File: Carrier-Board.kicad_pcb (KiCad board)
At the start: 4 copper layers, 92 x 96 mm, 59 parts, among them J1 CONN_3-6318491-6, J10 Conn_02x03_Odd_Even, J2 Conn_01x0, J4 SI-51009-F, J6 Conn_01x03_Male, J7 Conn_01x03_Male, J8 Conn_01x06_Male, J9 Conn_02x04_Odd_Even, SW1 SW_Push, SW2 SW_Push, SW3 SW_Push, U1 MPM3620, U2 MPM3620, m1 MountingHole_2.7mm_M2.5_Pad, m2 MountingHole_2.7mm_M2.5_Pad

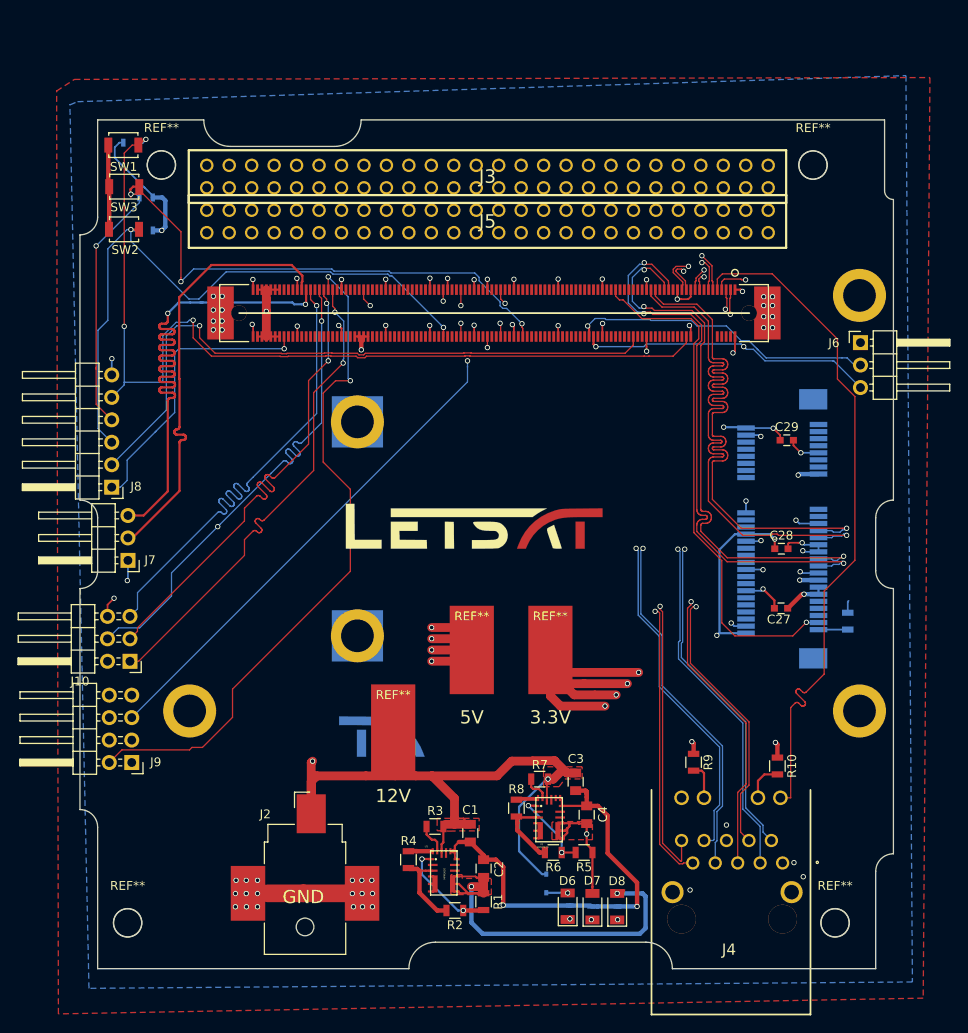
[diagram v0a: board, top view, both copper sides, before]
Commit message: Finished USB>rs232
Verify needed
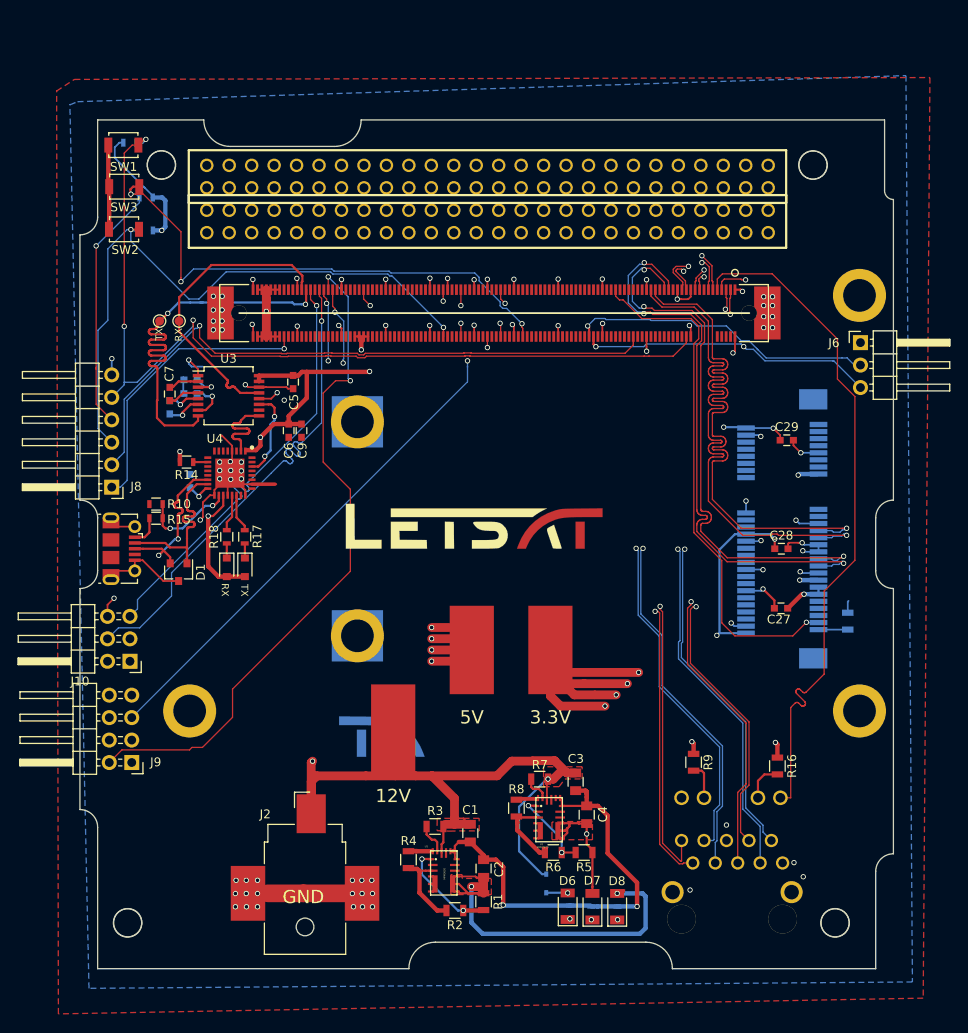
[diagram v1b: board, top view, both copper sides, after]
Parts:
- removed J7: Conn_01x03_Male, Pin_Headers:Pin_Header_Angled_1x03_Pitch2.54mm
- added C10: .1uF, Capacitors_SMD:C_0603, B.Cu at (94.4, 64.8)
- added C11: .33uF, Capacitors_SMD:C_0603, B.Cu at (94.4, 53.4)
- added C12: .33uF, Capacitors_SMD:C_0603, B.Cu at (94.4, 55.0)
- added C5: .1uF, Capacitors_SMD:C_0603, F.Cu at (106.0, 53.6)
- added C6: .1uF, Capacitors_SMD:C_0603, F.Cu at (105.5, 59.1)
- added C7: 47nF, Capacitors_SMD:C_0603, F.Cu at (92.1, 55.0)
- added C8: .33uF, Capacitors_SMD:C_0603, B.Cu at (92.1, 56.5)
- added C9: 4.7uF, Capacitors_SMD:C_0603, F.Cu at (107.0, 59.1)
- added D1: PESD12VL2BT,215, Diodes_SMD:D_SOT-23_NKA, F.Cu at (93.1, 75.2)
- added D2: LED, Diodes_SMD:D_0805, F.Cu at (100.6, 74.6)
- added D3: LED, Diodes_SMD:D_0805, F.Cu at (98.5, 74.6)
- added J11: USB_B_Micro, Connectors_USB:USB_Micro-B_Molex-105017-0001, F.Cu at (85.8, 72.5)
- added R10: 10K, Resistors_SMD:R_0603, F.Cu at (90.5, 67.5)
- added R14: 10K, Resistors_SMD:R_0603, F.Cu at (94.0, 62.7)
- added R15: 4.7K, Resistors_SMD:R_0603, F.Cu at (90.5, 69.0)
- added R17: 200, Resistors_SMD:R_0603, F.Cu at (100.6, 71.2)
- added R18: 200, Resistors_SMD:R_0603, F.Cu at (98.5, 71.2)
- added REF**: TestPoint_Pad_D1.0mm, TestPoint:TestPoint_Pad_D1.0mm, F.Cu at (93.1, 46.8)
- added REF**: TestPoint_Pad_D1.0mm, TestPoint:TestPoint_Pad_D1.0mm, F.Cu at (90.9, 46.8)
- added U3: MAX3221, Housings_SSOP:SSOP-16_5.3x6.2mm_Pitch0.65mm, F.Cu at (98.7, 55.2)
- added U4: FT232RQ, FT232RQ:QFN50P500X500X100-33N, F.Cu at (98.9, 64.0)
- J3, J5: value (none) -> Conn_02x26_Odd_Even
- U9: value (none) -> MSATA-Socket
- renumbered R10 to R16
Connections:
- C27 pad 1: +3.3V -> Net-(C27-Pad1)
- C28 pad 1: +3.3V -> Net-(C28-Pad1)
- C29 pad 1: +3.3V -> Net-(C29-Pad1)
- J1 pad 223: GBE0_CTREF(GND) -> (no net)
- J1 pad 224: GBE0_CTREF(GND) -> (no net)
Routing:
- net mCOM_5V_SBY: track 182.1 -> 245.1 mm, vias 8 -> 12
- net GBE0_CTREF(GND): track 191.3 -> 234.0 mm, vias 84 -> 81
- net Net-(D1-Pad1): track 0.00 -> 22.0 mm
- net Net-(D1-Pad2): track 0.00 -> 19.2 mm, vias 0 -> 2
- net mCOM_TX: track 64.6 -> 47.7 mm
- net mCOM_RX: track 48.9 -> 34.0 mm
- net Reset#: track 0.00 -> 10.7 mm, vias 0 -> 2
- net RXD: track 0.00 -> 10.4 mm
- net TXD: track 0.00 -> 10.0 mm, vias 0 -> 2
- net (no net): track 0.00 -> 6.57 mm, vias 0 -> 16
- net SPI_CS#: track 55.2 -> 49.1 mm
- net Net-(C12-Pad1): track 0.00 -> 4.56 mm, vias 0 -> 1
- net Net-(R17-Pad2): track 0.00 -> 4.34 mm
- net Net-(R18-Pad2): track 0.00 -> 4.20 mm
- net Net-(C8-Pad2): track 0.00 -> 3.96 mm, vias 0 -> 1
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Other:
- board text added: "RX"
- board text added: "TX"

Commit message: changed serial number
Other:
- board text added: "S/N: 0C137_v2"
- board text removed: "S/N: 0C137"

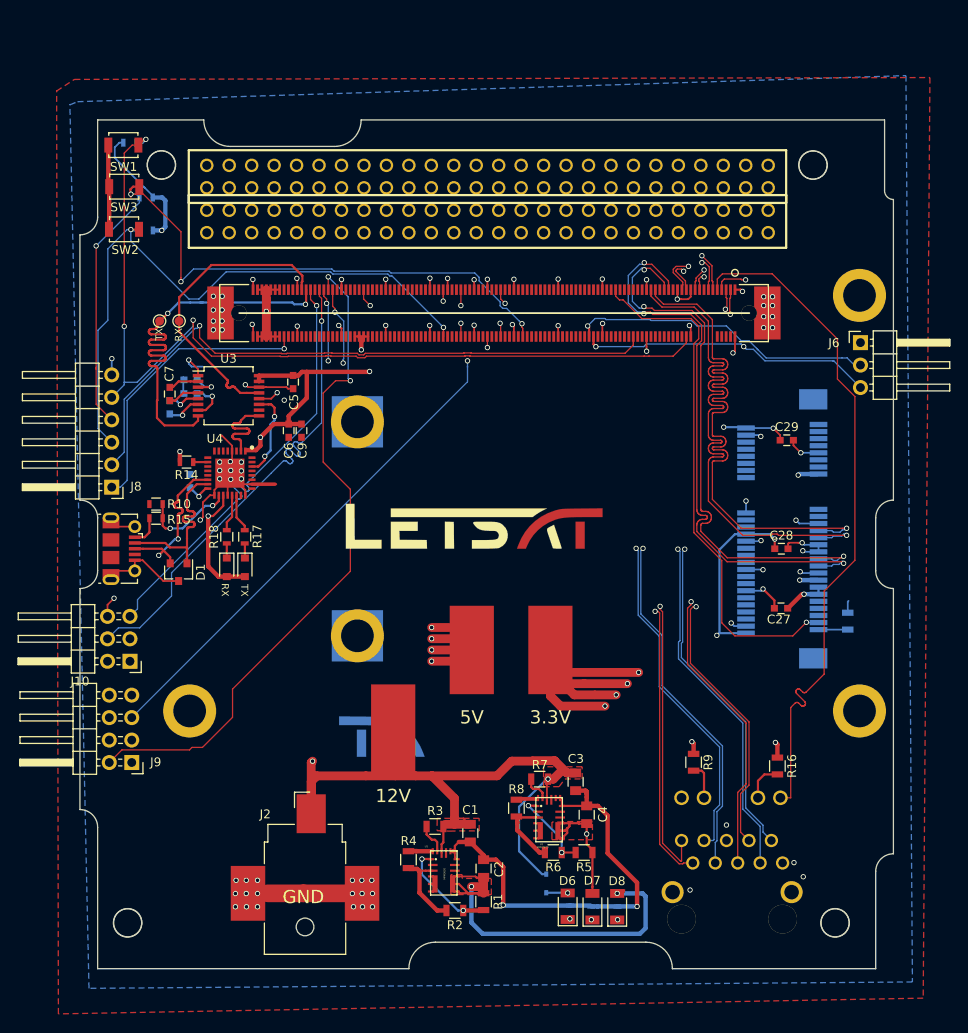
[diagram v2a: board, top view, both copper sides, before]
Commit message: Change footprint sizes
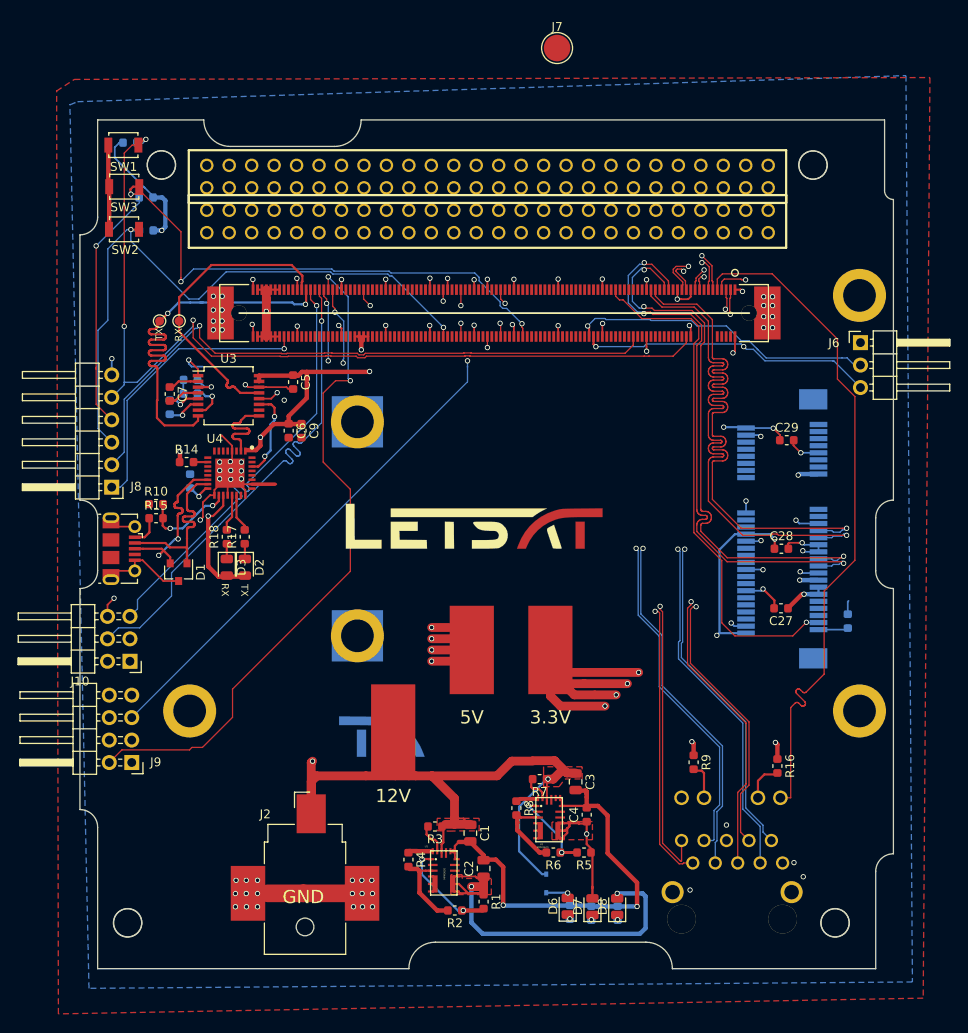
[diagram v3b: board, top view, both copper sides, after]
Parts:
- added J7: Conn_01x03_Male, TestPoint:TestPoint_Pad_D3.0mm, F.Cu at (135.9, 15.9)
- C1, C2, C3: footprint Capacitors_SMD:C_0805 -> Capacitor_SMD:C_0805_2012Metric
- C10, C11, C12, C27, C28, C29, C5, C6, C7, C8, C9: footprint Capacitors_SMD:C_0603 -> Capacitor_SMD:C_0603_1608Metric
- C4: footprint Capacitors_SMD:C_0805 -> Capacitor_SMD:C_0603_1608Metric
- D2, D3: footprint Diodes_SMD:D_0805 -> Diode_SMD:D_0805_2012Metric
- D6, D7, D8: footprint Diodes_SMD:D_1206 -> Diode_SMD:D_0805_2012Metric
- G1: footprint BusSimulator:LetSatLogo440 -> Carrier-Board:LetSat_Logo_440
- J1: footprint BusSimulator:ComExpressMini10 -> Carrier-Board:ComExpressMini10
- R1, R16, R2, R3, R32, R4, R5, R6, R7, R8, R9: footprint Resistors_SMD:R_0805 -> Resistor_SMD:R_0603_1608Metric
- R10, R11, R12, R13, R14, R15, R17, R18, R23, R24, R25: footprint Resistors_SMD:R_0603 -> Resistor_SMD:R_0603_1608Metric
- U1, U2: footprint BusSimulator:QFN-20 -> Carrier-Board:QFN-20
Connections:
- C27 pad 1: Net-(C27-Pad1) -> +3.3V
- C28 pad 1: Net-(C28-Pad1) -> +3.3V
- C29 pad 1: Net-(C29-Pad1) -> +3.3V
- J2 pad 3: GBE0_CTREF(GND) -> (no net)
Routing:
- net mCOM_12V: track 148.1 -> 155.2 mm
- net Net-(R5-Pad2): track 9.35 -> 11.3 mm
- net mCOM_5V_SBY: track 245.1 -> 243.8 mm
- net GNDA: track 19.7 -> 21.0 mm
- net +3.3V: track 245.6 -> 246.8 mm
- net Net-(R8-Pad1): track 5.00 -> 5.61 mm
- net Net-(D6-Pad1): track 0.00 -> 0.59 mm
- net Net-(D7-Pad1): track 0.00 -> 0.59 mm
- net Net-(D5-Pad2): track 2.44 -> 3.00 mm
- net Net-(D8-Pad1): track 0.00 -> 0.56 mm
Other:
- net class Default: clearance 0.2 -> 0.15
- net class Power: clearance 0.2 -> 0.15
- net class Signal: clearance 0.2 -> 0.15
- rule trace_clearance: 0.2 -> 0.15

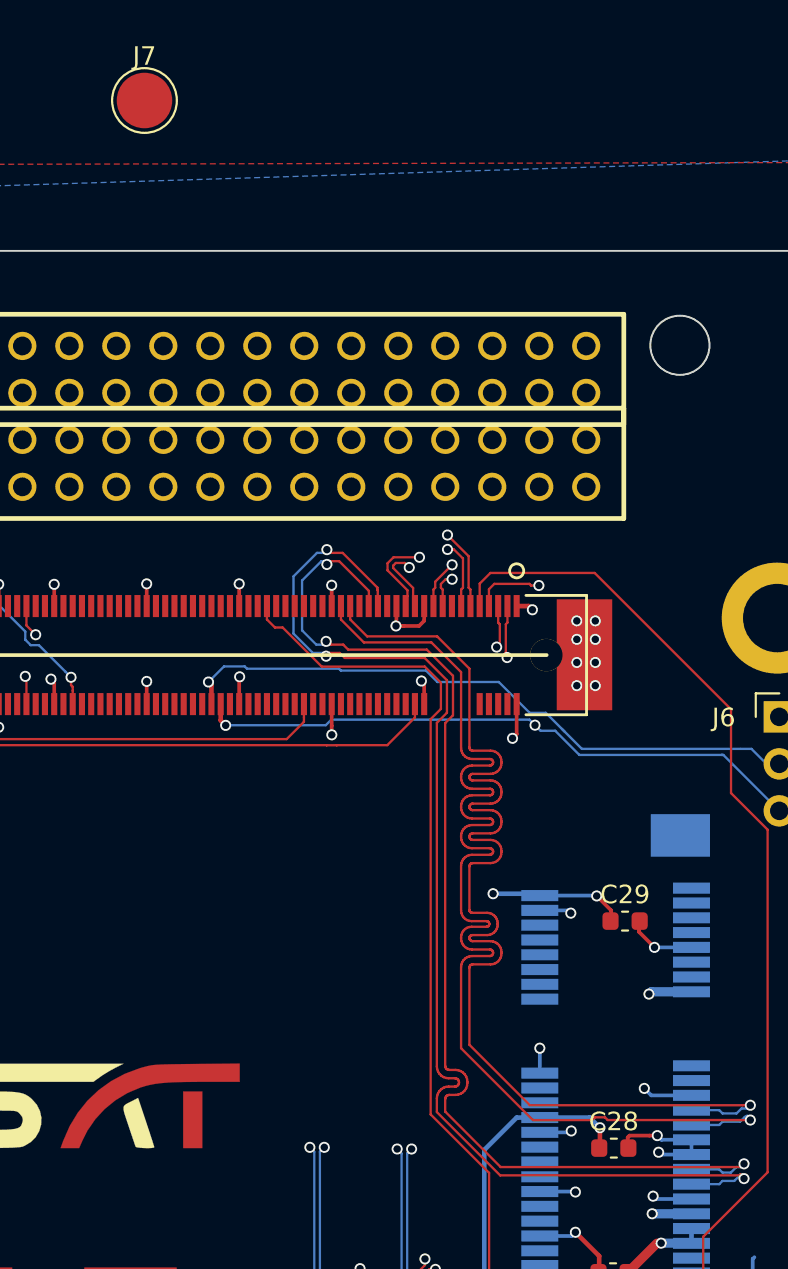
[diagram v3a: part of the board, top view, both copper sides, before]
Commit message: added 3d models
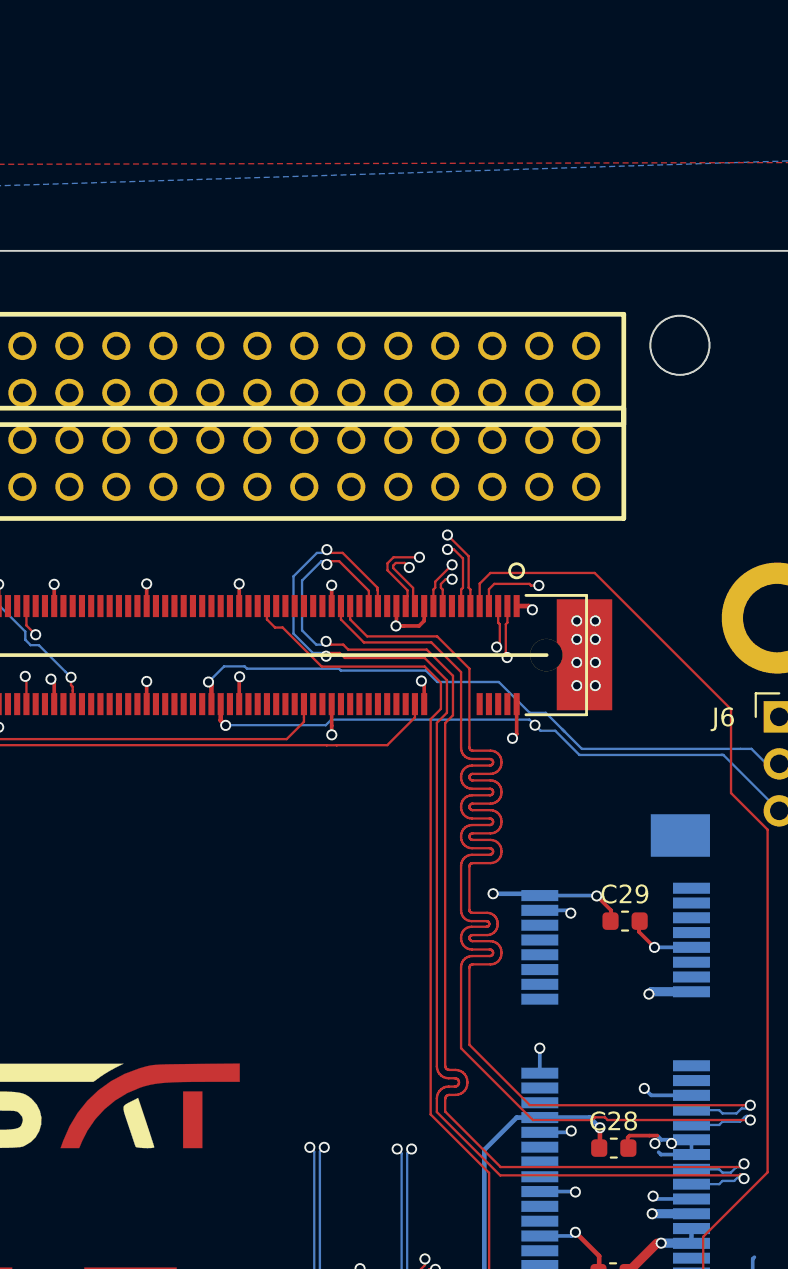
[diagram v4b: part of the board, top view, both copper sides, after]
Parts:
- removed J7: Conn_01x03_Male, TestPoint:TestPoint_Pad_D3.0mm
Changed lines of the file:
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@@
-(kicad_pcb (version 20171130) (host pcbnew 5.0.0)
+(kicad_pcb (version 20171130) (host pcbnew "(5.0.0-rc2-dev-789-g6f249e5eb)")
   (general
     (thickness 1.6)
@@
     (tracks 4006)
     (zones 0)
-    (modules 80)
+    (modules 79)
     (nets 371)
   )
@@
       (hpglpennumber 1)
       (hpglpenspeed 20)
-      (hpglpendiameter 15.000000)
+      (hpglpendiameter 15)
       (psnegative false)
       (psa4output false)
@@
       (drillshape 0)
       (scaleselection 1)
-      (outputdirectory "FinalProtoCarrier/"))
+      (outputdirectory FinalProtoCarrier/))
   )
   (net 0 "")
@@
     (pad 1 thru_hole circle (at 5.84 -17.14 90) (size 1.5 1.5) (drill 0.97) (layers *.Cu *.Mask F.SilkS)
       (net 38 "GBE0_CTREF(GND)"))
+    (model ${KIPRJMOD}/480251190.stp
+      (offset (xyz 0 12.5 5.5))
+      (scale (xyz 1 1 1))
+      (rotate (xyz -90 0 0))
+    )
   )
   (module Diodes_SMD:D_SOD-323 (layer B.Cu)
@@
       (rotate (xyz 0 0 0))
     )
-  )
-  (module TestPoint:TestPoint_Pad_D3.0mm (layer F.Cu)
-    (at 135.880001 15.871001)
-    (descr "SMD pad as test Point, diameter 3.0mm")
-    (tags "test point SMD pad")
-    (attr virtual)
-    (fp_text reference J7 (at 0 -2.398) (layer F.SilkS)
-      (effects (font (size 1 1) (thickness 0.15)))
-    )
-    (fp_text value Conn_01x03_Male (at 0 2.55) (layer F.Fab)
-      (effects (font (size 1 1) (thickness 0.15)))
-    )
-    (fp_text user %R (at 0 -2.4) (layer F.Fab)
-      (effects (font (size 1 1) (thickness 0.15)))
+    (model ${KIPRJMOD}/Mcom5mm.stp
+      (offset (xyz 34.7 -2.5 4.5))
+      (scale (xyz 1 1 1))
+      (rotate (xyz 0 0 0))
     )
-    (fp_circle (center 0 0) (end 2 0) (layer F.CrtYd) (width 0.05))
-    (fp_circle (center 0 0) (end 0 1.75) (layer F.SilkS) (width 0.12))
-    (pad 1 smd circle (at 0 0) (size 3 3) (layers F.Cu F.Mask)
-      (net 38 "GBE0_CTREF(GND)"))
   )
   (module Resistor_SMD:R_0603_1608Metric (layer F.Cu)
@@
   (segment (start 165.45 72.85) (end 163.8 72.85) (width 0.2) (layer B.Cu) (net 38))
   (segment (start 163.8 72.85) (end 163.675 72.725) (width 0.2) (layer B.Cu) (net 38))
-  (via (at 163.675 72.725) (size 0.6) (drill 0.4) (layers F.Cu B.Cu) (net 38))
+  (via (at 163.475 72.25) (size 0.6) (drill 0.4) (layers F.Cu B.Cu) (net 38))
   (segment (start 165.45 72.05) (end 163.825 72.05) (width 0.2) (layer B.Cu) (net 38))
   (segment (start 163.825 72.05) (end 163.6 71.825) (width 0.2) (layer B.Cu) (net 38))
-  (via (at 163.6 71.825) (size 0.6) (drill 0.4) (layers F.Cu B.Cu) (net 38))
+  (via (at 164.375 72.25) (size 0.6) (drill 0.4) (layers F.Cu B.Cu) (net 38))
   (segment (start 165.45 69.65) (end 163.275 69.65) (width 0.2) (layer B.Cu) (net 38))
   (segment (start 163.275 69.65) (end 162.9 69.275) (width 0.2) (layer B.Cu) (net 38))
